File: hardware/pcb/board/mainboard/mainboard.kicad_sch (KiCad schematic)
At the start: 136 parts, among them J1 Conn_Coaxial, J10 USB_C_Receptacle, J11 2908-05WB-MG, J2 USB_C_Receptacle_USB2.0_16P, J3 Conn_02x35_Odd_Even_MountingP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, J4 Conn_02x40_Odd_Even_MountingP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, J5 Conn_02x40_Odd_Even_MountingP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, J7 Conn_01x30, J8 Conn_01x30, J9 Conn_01x30, Q1 BSS138, Q2 DMN3008SFG, Q3 DMN3008SFG, U1 TPS7A20_SOT-23, U11 TPS7A20_SOT-23, U12 AP33771C, U13 TXS0104E, U14 FT234XD-R, U2 LSM6DS3TR, U3 NEO-M8N, U4 BQ25606, U5 BQ27441-G1, U6 SN74LVC1T45DBVR, U7 LIS2MDL, U8 SN74LVC1T45DBVR, U9 TPS61235P

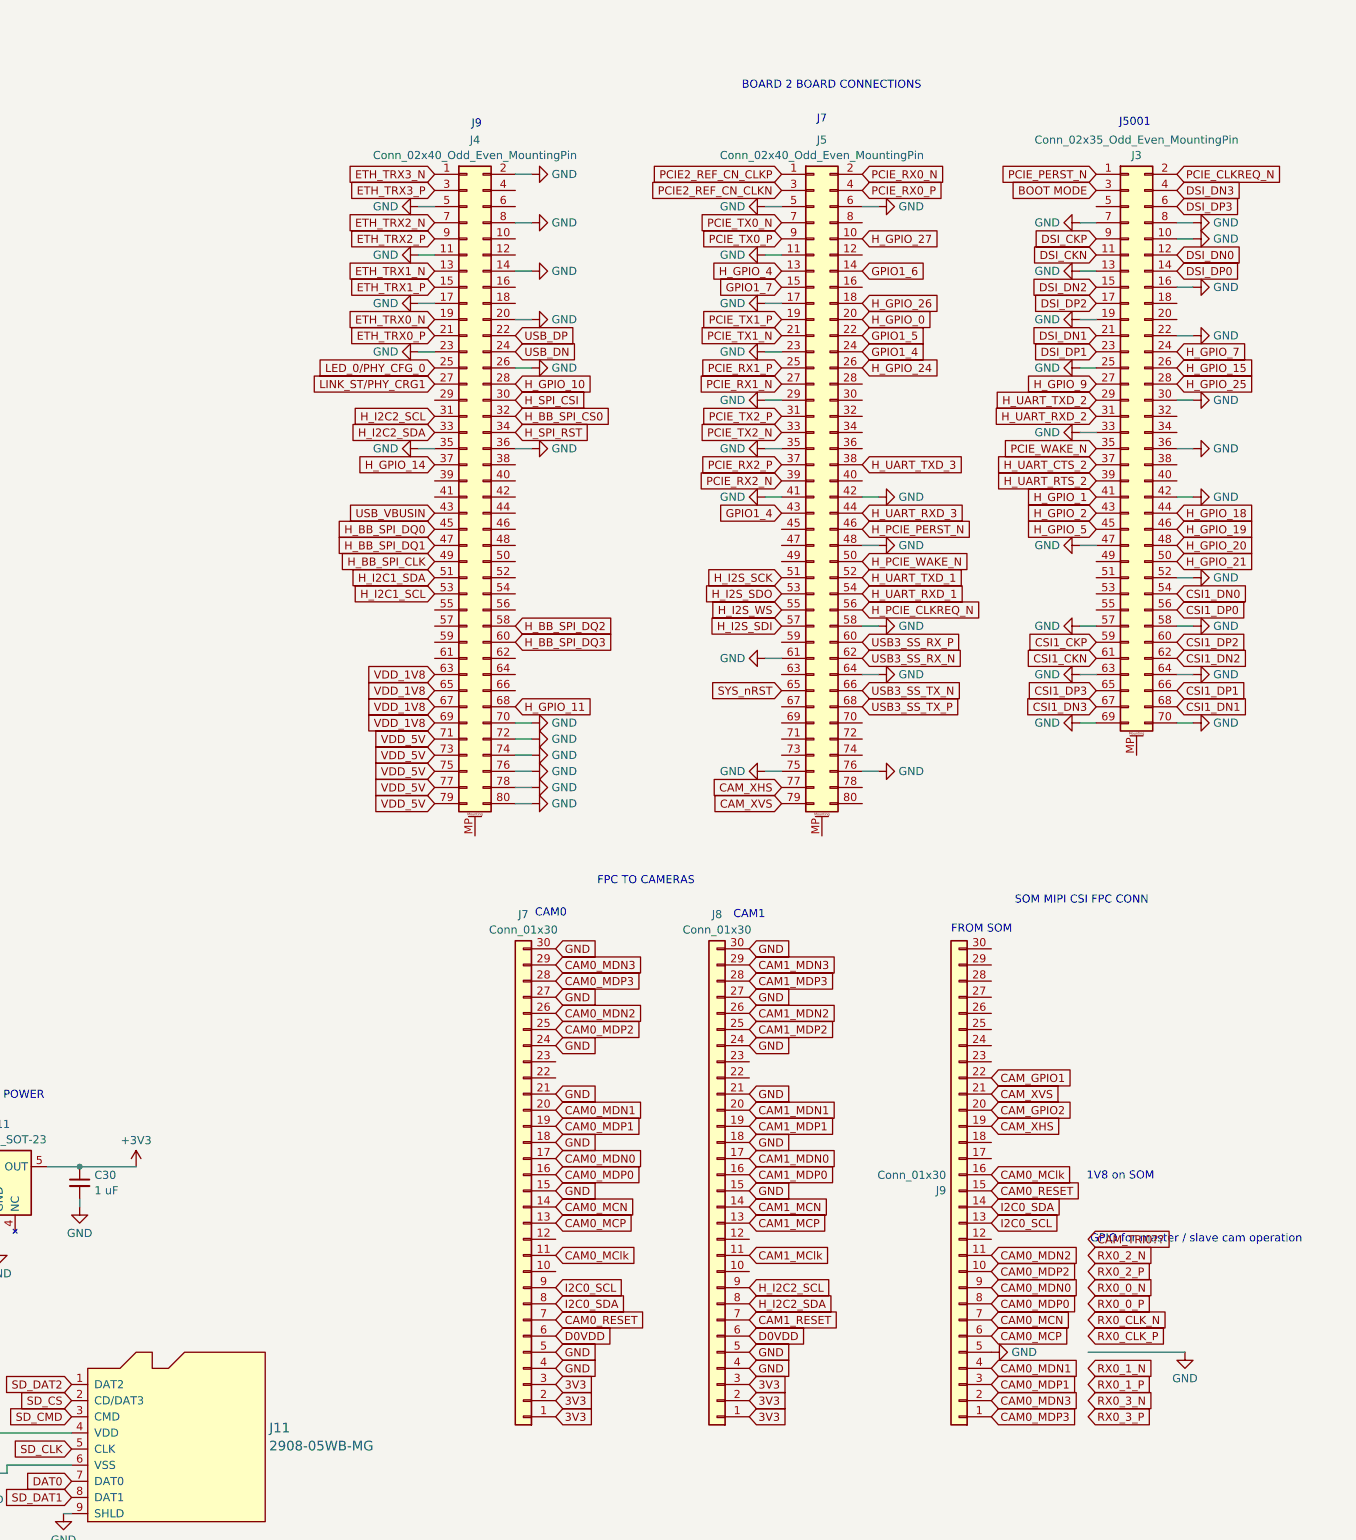
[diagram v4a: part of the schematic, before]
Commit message: change MIPI CSI location according to new schematics
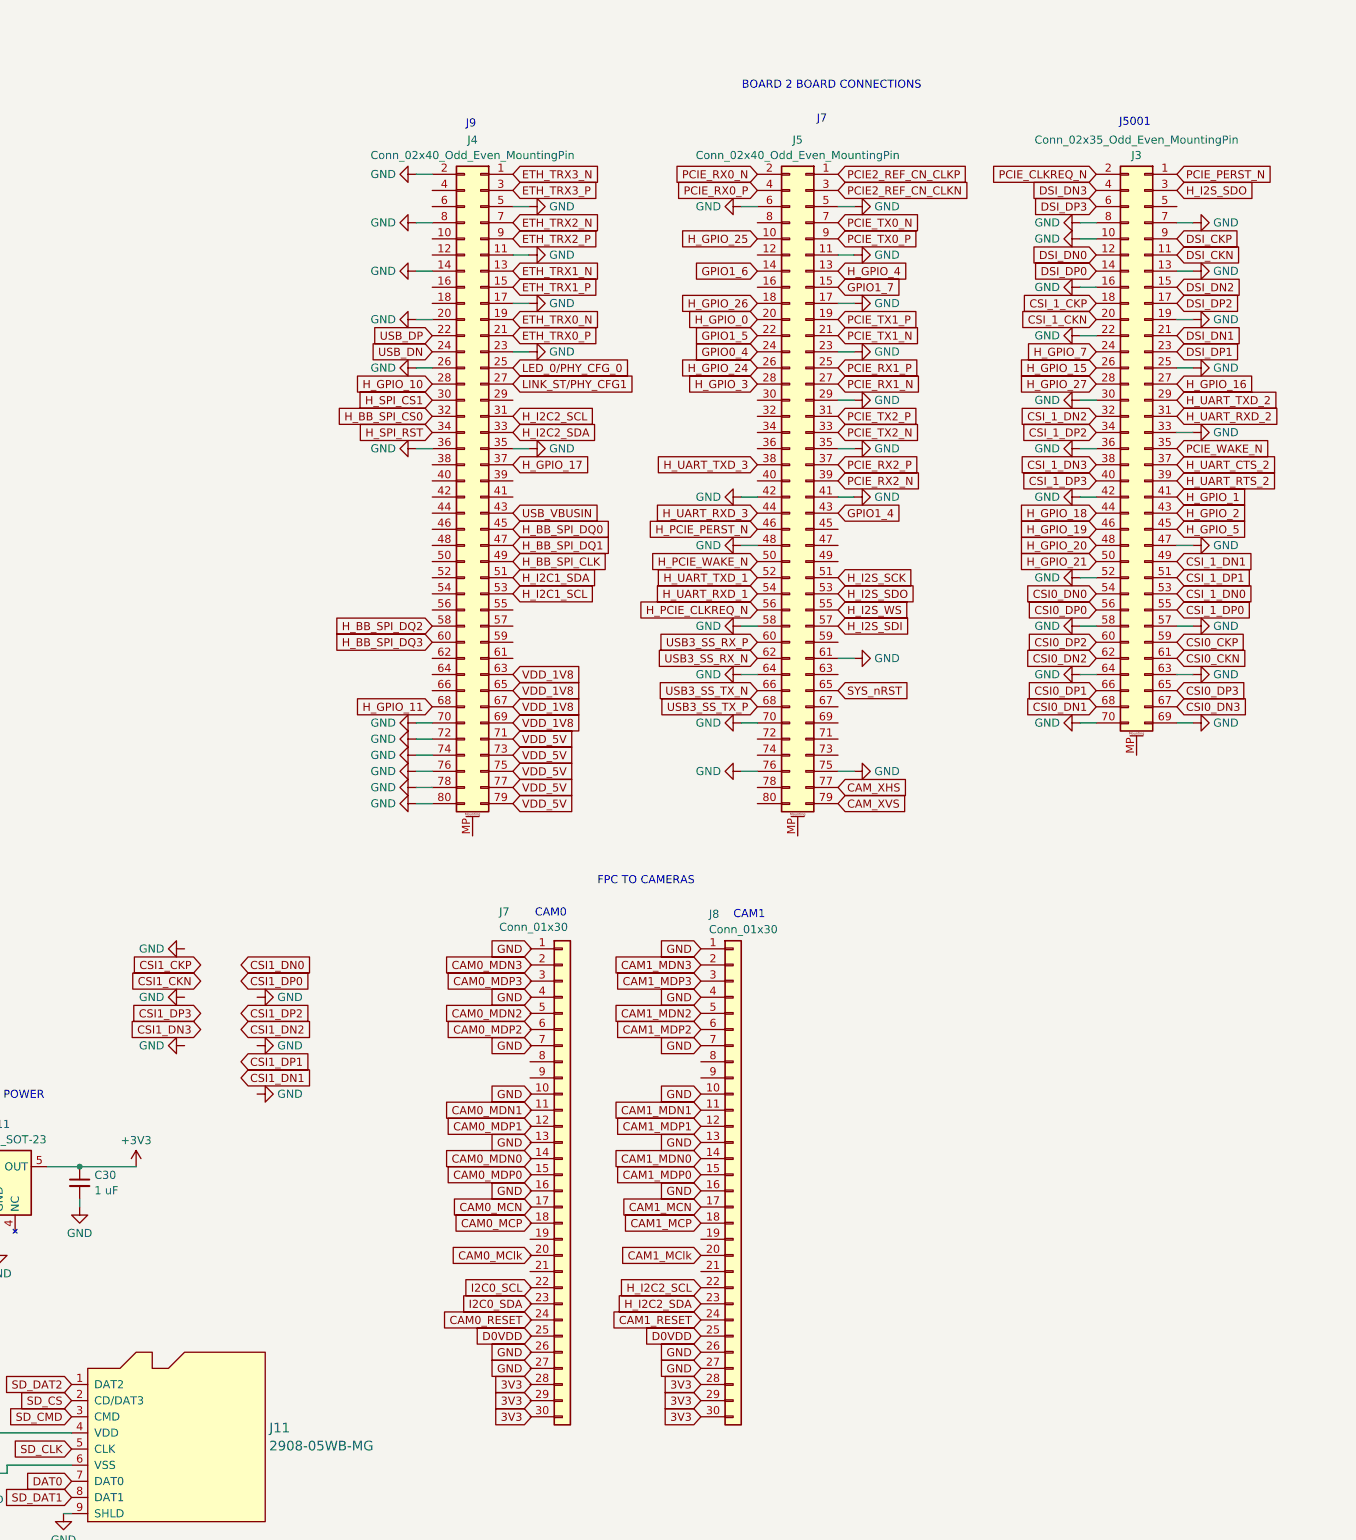
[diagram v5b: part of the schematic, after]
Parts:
- removed J9: Conn_01x30, Connector_FFC-FPC:Hirose_FH12-30S-0.5SH_1x30-1MP_P0.50mm_Horizontal, symbol Connector_Generic:Conn_01x30
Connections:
- net BOOT MODE is gone; now on net H_I2S_SDO: J3.3 (Pin_3)
- net 3V3: now also J8.28 (Pin_28), J8.29 (Pin_29), J8.30 (Pin_30); no longer J7.1 (Pin_1), J7.2 (Pin_2), J7.3 (Pin_3), J8.1 (Pin_1), J8.2 (Pin_2), J8.3 (Pin_3)
- net CAM0_MCN: no longer J7.14 (Pin_14)
- net CAM0_MCP: no longer J7.13 (Pin_13)
- net CAM0_MClk: no longer J7.11 (Pin_11)
- net CAM0_MDN0: no longer J7.17 (Pin_17)
- net CAM0_MDN1: no longer J7.20 (Pin_20)
- net CAM0_MDN2: no longer J7.26 (Pin_26)
- net CAM0_MDN3: no longer J7.29 (Pin_29)
- net CAM0_MDP0: no longer J7.16 (Pin_16)
- net CAM0_MDP1: no longer J7.19 (Pin_19)
- net CAM0_MDP2: no longer J7.25 (Pin_25)
- net CAM0_MDP3: no longer J7.28 (Pin_28)
- net CAM0_RESET: no longer J7.7 (Pin_7)
- net CAM1_MCN: now also J8.17 (Pin_17); no longer J8.14 (Pin_14)
- net CAM1_MCP: now also J8.18 (Pin_18); no longer J8.13 (Pin_13)
- net CAM1_MClk: now also J8.20 (Pin_20); no longer J8.11 (Pin_11)
- net CAM1_MDN0: now also J8.14 (Pin_14); no longer J8.17 (Pin_17)
- net CAM1_MDN1: now also J8.11 (Pin_11); no longer J8.20 (Pin_20)
- net CAM1_MDN2: now also J8.5 (Pin_5); no longer J8.26 (Pin_26)
- net CAM1_MDN3: now also J8.2 (Pin_2); no longer J8.29 (Pin_29)
- net CAM1_MDP0: now also J8.15 (Pin_15); no longer J8.16 (Pin_16)
- net CAM1_MDP1: now also J8.12 (Pin_12); no longer J8.19 (Pin_19)
- net CAM1_MDP2: now also J8.6 (Pin_6); no longer J8.25 (Pin_25)
- net CAM1_MDP3: now also J8.3 (Pin_3); no longer J8.28 (Pin_28)
- net CAM1_RESET: now also J8.24 (Pin_24); no longer J8.7 (Pin_7)
- net CSI1_CKN: no longer J3.61 (Pin_61)
- net CSI1_CKP: no longer J3.59 (Pin_59)
- net CSI1_DN0: no longer J3.54 (Pin_54)
- net CSI1_DN1: no longer J3.68 (Pin_68)
- net CSI1_DN2: no longer J3.62 (Pin_62)
- net CSI1_DN3: no longer J3.67 (Pin_67)
- net CSI1_DP0: no longer J3.56 (Pin_56)
- net CSI1_DP1: no longer J3.66 (Pin_66)
- net CSI1_DP2: no longer J3.60 (Pin_60)
- net CSI1_DP3: no longer J3.65 (Pin_65)
- net D0VDD: now also J8.25 (Pin_25); no longer J7.6 (Pin_6), J8.6 (Pin_6)
- net GND: now also J5.70 (Pin_70), J8.1 (Pin_1), J8.10 (Pin_10), J8.13 (Pin_13), J8.16 (Pin_16), J8.26 (Pin_26), J8.7 (Pin_7); no longer J7.15 (Pin_15), J7.18 (Pin_18), J7.21 (Pin_21), J7.24 (Pin_24), J7.27 (Pin_27), J7.30 (Pin_30), J7.4 (Pin_4), J7.5 (Pin_5), J8.15 (Pin_15), J8.18 (Pin_18), J8.21 (Pin_21), J8.24 (Pin_24), J8.30 (Pin_30), J8.5 (Pin_5)
- net GPIO1_4: no longer J5.24 (Pin_24)
- net H_GPIO_25: now also J5.10 (Pin_10); no longer J3.28 (Pin_28)
- net H_GPIO_27: now also J3.28 (Pin_28); no longer J5.10 (Pin_10)
- net H_I2C2_SCL: now also J8.22 (Pin_22); no longer J8.9 (Pin_9)
- net H_I2C2_SDA: now also J8.23 (Pin_23); no longer J8.8 (Pin_8)
- net I2C0_SCL: no longer J7.9 (Pin_9)
- net I2C0_SDA: no longer J7.8 (Pin_8)
- net CSI_1_CKP: now reaches J3.18 (Pin_18)
- net CSI_1_CKN: now reaches J3.20 (Pin_20)
- net CSI_1_DN2: now reaches J3.32 (Pin_32)
- net CSI_1_DP2: now reaches J3.34 (Pin_34)
- net CSI_1_DN3: now reaches J3.38 (Pin_38)
- net CSI_1_DP3: now reaches J3.40 (Pin_40)
- net CSI_1_DN1: now reaches J3.49 (Pin_49)
- net CSI_1_DP1: now reaches J3.51 (Pin_51)
- net CSI_1_DN0: now reaches J3.53 (Pin_53)
- net CSI_1_DP0: now reaches J3.55 (Pin_55)
- net H_GPIO_3: now reaches J5.28 (Pin_28)
- net H_GPIO_14 renamed H_GPIO_17
- net H_GPIO_9 renamed H_GPIO_16
- net H_SPI_CSI renamed H_SPI_CS1
- net LINK_ST/PHY_CRG1 renamed LINK_ST/PHY_CFG1
- new net CSI0_CKN: J3.61 (Pin_61)
- new net CSI0_CKP: J3.59 (Pin_59)
- new net CSI0_DN0: J3.54 (Pin_54)
- new net CSI0_DN1: J3.68 (Pin_68)
- new net CSI0_DN2: J3.62 (Pin_62)
- new net CSI0_DN3: J3.67 (Pin_67)
- new net CSI0_DP0: J3.56 (Pin_56)
- new net CSI0_DP1: J3.66 (Pin_66)
- new net CSI0_DP2: J3.60 (Pin_60)
- new net CSI0_DP3: J3.65 (Pin_65)
- new net GPIO0_4: J5.24 (Pin_24)
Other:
- note removed: "1V8 on SOM"
- note removed: "FROM SOM"
- note removed: "GPIO for master / slave cam operation"
- note removed: "SOM MIPI CSI FPC CONN"
- moved on the sheet: J5, J7, J8

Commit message: new 3V3 setup for cameras, 30 pin mipi connections
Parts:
- removed C29, C30: 1 uF, Capacitor_SMD:C_0603_1608Metric, symbol Device:C_Small
- removed U11: TPS7A20_SOT-23, Package_SON:Texas_X2SON-4_1x1mm_P0.65mm, symbol unsurv_offline_pcb_symbols:TPS7A20_SOT-23
- added C43, C44, C45, C46: 4.7 uF, Capacitor_SMD:C_0603_1608Metric, symbol Device:C_Small
- added R21, R33, R36: 0, Resistor_SMD:R_0603_1608Metric, symbol Device:R_Small
- added R34, R35: 10k, Resistor_SMD:R_0603_1608Metric, symbol Device:R_Small
- added U10, U11: AP2114H-3_3TRG1, digikey-footprints:SOT-223, symbol dk_PMIC-Voltage-Regulators-Linear:AP2114H-3_3TRG1
- added Y1, Y2: SiT8008xx-1x-xxE, Oscillator:Oscillator_SMD_SiT_PQFN-4Pin_2.5x2.0mm, symbol Oscillator:SiT8008xx-1x-xxE
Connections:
- net CAM1_RESET is gone; now on net CAM0_RESET: J8.24 (Pin_24)
- net H_GPIO_19 is gone; now on net CAM0_RESET: J3.46 (Pin_46)
- net VDD_5V is gone; now on net +5V: J4.71 (Pin_71), J4.73 (Pin_73), J4.75 (Pin_75), J4.77 (Pin_77), J4.79 (Pin_79)
- net +5V: now also C43.1, C45.1, U10.3 (IN), U11.3 (IN)
- net CAM0_MClk: now also J7.20 (Pin_20), R21.2
- net CAM0_RESET: now also R34.1, R35.2, R36.1
- net CAM1_MCN: no longer J8.17 (Pin_17)
- net CAM1_MCP: no longer J8.18 (Pin_18)
- net CAM1_MClk: now also R33.2
- net CAM1_MDN0: no longer J8.14 (Pin_14)
- net CAM1_MDN1: no longer J8.11 (Pin_11)
- net CAM1_MDN2: no longer J8.5 (Pin_5)
- net CAM1_MDN3: no longer J8.2 (Pin_2)
- net CAM1_MDP0: no longer J8.15 (Pin_15)
- net CAM1_MDP1: no longer J8.12 (Pin_12)
- net CAM1_MDP2: no longer J8.6 (Pin_6)
- net CAM1_MDP3: no longer J8.3 (Pin_3)
- net CSI0_CKN: now also J7.17 (Pin_17)
- net CSI0_CKP: now also J7.18 (Pin_18)
- net CSI0_DN0: now also J7.14 (Pin_14)
- net CSI0_DN1: now also J7.11 (Pin_11)
- net CSI0_DN2: now also J7.5 (Pin_5)
- net CSI0_DN3: now also J7.2 (Pin_2)
- net CSI0_DP0: now also J7.15 (Pin_15)
- net CSI0_DP1: now also J7.12 (Pin_12)
- net CSI0_DP2: now also J7.6 (Pin_6)
- net CSI0_DP3: now also J7.3 (Pin_3)
- net CSI_1_CKN: now also J8.17 (Pin_17)
- net CSI_1_CKP: now also J8.18 (Pin_18)
- net CSI_1_DN0: now also J8.14 (Pin_14)
- net CSI_1_DN1: now also J8.11 (Pin_11)
- net CSI_1_DN2: now also J8.5 (Pin_5)
- net CSI_1_DN3: now also J8.2 (Pin_2)
- net CSI_1_DP0: now also J8.15 (Pin_15)
- net CSI_1_DP1: now also J8.12 (Pin_12)
- net CSI_1_DP2: now also J8.6 (Pin_6)
- net CSI_1_DP3: now also J8.3 (Pin_3)
- net D0VDD: no longer J8.25 (Pin_25)
- net GND: now also J7.1 (Pin_1), J7.10 (Pin_10), J7.13 (Pin_13), J7.16 (Pin_16), J7.26 (Pin_26), J7.27 (Pin_27), J7.4 (Pin_4), J7.7 (Pin_7), C43.2, C44.2, C45.2, C46.2, R35.1, U10.1 (GND), U11.1 (GND), Y1.2 (GND), Y2.2 (GND)
- net I2C0_SCL: now also J7.22 (Pin_22)
- net I2C0_SDA: now also J7.23 (Pin_23)
- net VDD_1V8: now also J7.25 (Pin_25), J8.25 (Pin_25), R34.2, Y1.1 (OE), Y1.4 (Vdd), Y2.1 (OE), Y2.4 (Vdd)
- net at J7.24 (Pin_24): now also R36.2
- net CAM0_3V3: now reaches J7.28 (Pin_28)
- net CAM0_3V3: now also J7.29 (Pin_29), J7.30 (Pin_30), C44.1, U10.2 (VOUT), U10.4 (VOUT)
- net 3V3 renamed CAM1_3V3
- net CAM1_3V3: now also C46.1, U11.2 (VOUT), U11.4 (VOUT)
- new net: R33.1, Y2.3 (OUT)
- new net: R21.1, Y1.3 (OUT)
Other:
- note added: "# TODO - check coax conn type for antennas - TP everything! - 0 ohm connections - add way for cam0 cam1 slave master operation? - TXS0102 logic lvl shifter - WATCH FOR INVERSE PINS WHEN SWITCHING SIDE FOR CAM 0 / 1 - transfer SOM based MIPI to CAM connection via FPC - CAM CLK crystal , 0 Ohm, 25 MHz, 25 ppm, 1.8V"
- note added: "CAM 3V3 POWER"
- note removed: "# TODO - check coax conn type for antennas - TP everything! - 0 ohm connections - add way for cam0 cam1 slave master operation? - TXS0102 logic lvl shifter - WATCH FOR INVERSE PINS WHEN SWITCHING SIDE FOR CAM 0 / 1 - transfer SOM based MIPI to CAM connection via FPC"
- note removed: "2nd 3V3 POWER"
- moved on the sheet: C37, J11, J8, R30, R31

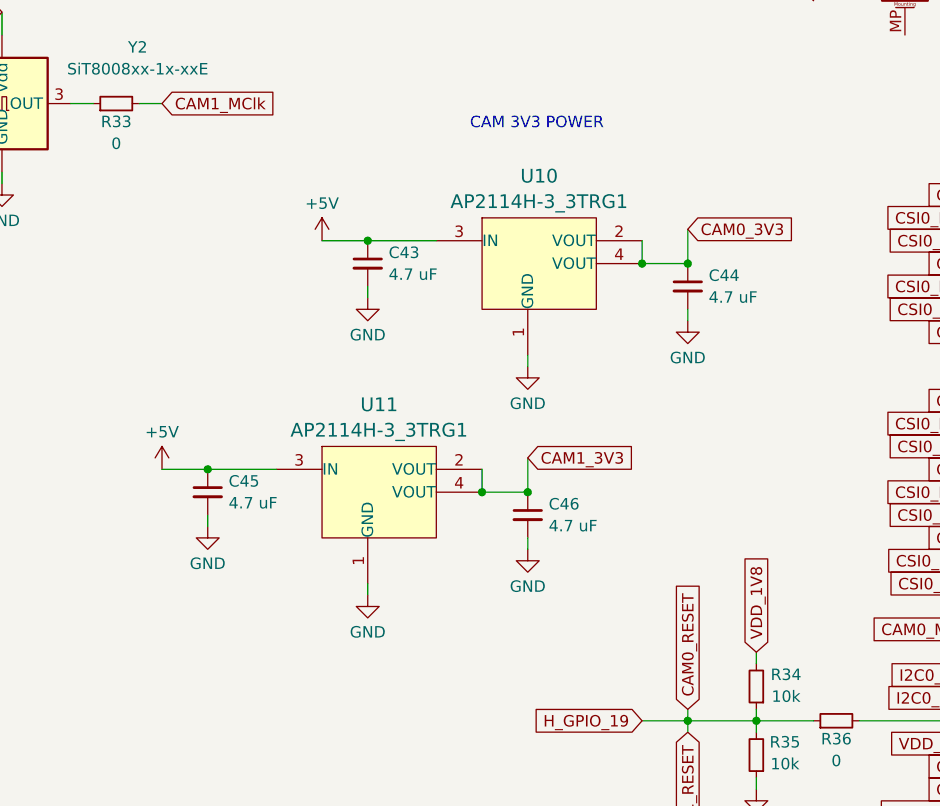
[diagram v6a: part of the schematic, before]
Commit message: place ment of new 3V3 + oscillators + reset mechanic
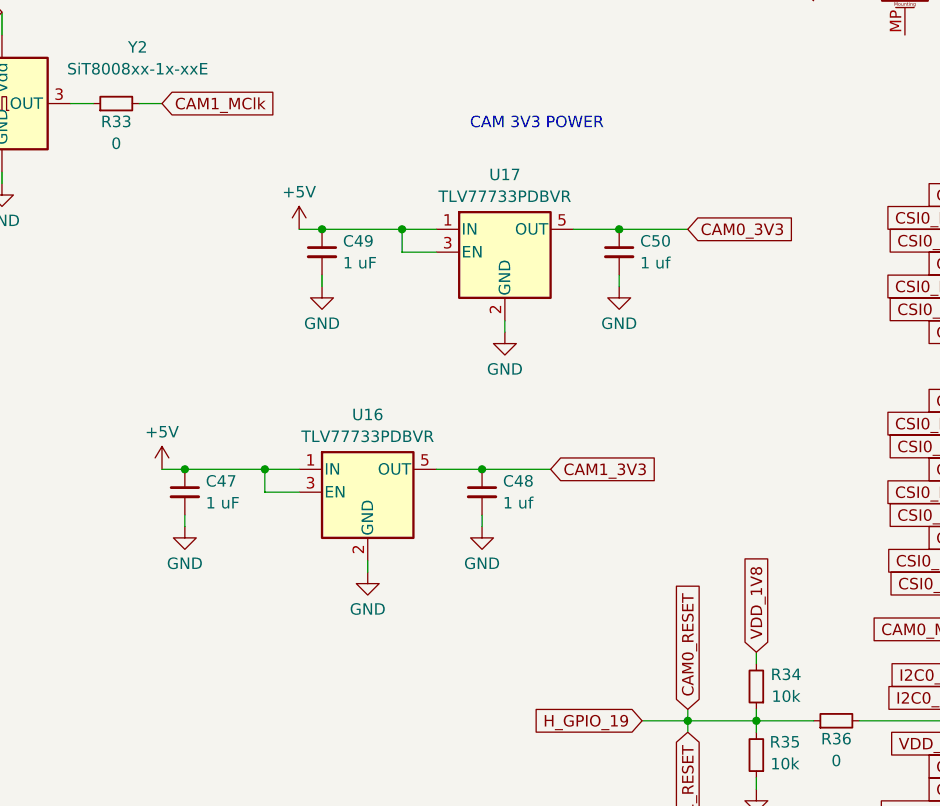
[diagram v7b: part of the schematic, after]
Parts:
- removed C43, C44, C45, C46: 4.7 uF, Capacitor_SMD:C_0603_1608Metric, symbol Device:C_Small
- removed U10, U11: AP2114H-3_3TRG1, digikey-footprints:SOT-223, symbol dk_PMIC-Voltage-Regulators-Linear:AP2114H-3_3TRG1
- added C47, C49: 1 uF, Capacitor_SMD:C_0603_1608Metric, symbol Device:C_Small
- added C48, C50: 1 uf, Capacitor_SMD:C_0603_1608Metric, symbol Device:C_Small
- added U16, U17: TLV77733PDBVR, Package_TO_SOT_SMD:SOT-23-5, symbol Regulator_Linear:TLV70032_SOT23-5
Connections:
- net +5V: now also C47.1, C49.1, U16.1 (IN), U16.3 (EN), U17.1 (IN), U17.3 (EN)
- net CAM0_3V3: now also C50.1, U17.5 (OUT)
- net CAM1_3V3: now also C48.1, U16.5 (OUT)
- net GND: now also C47.2, C48.2, C49.2, C50.2, U16.2 (GND), U17.2 (GND)

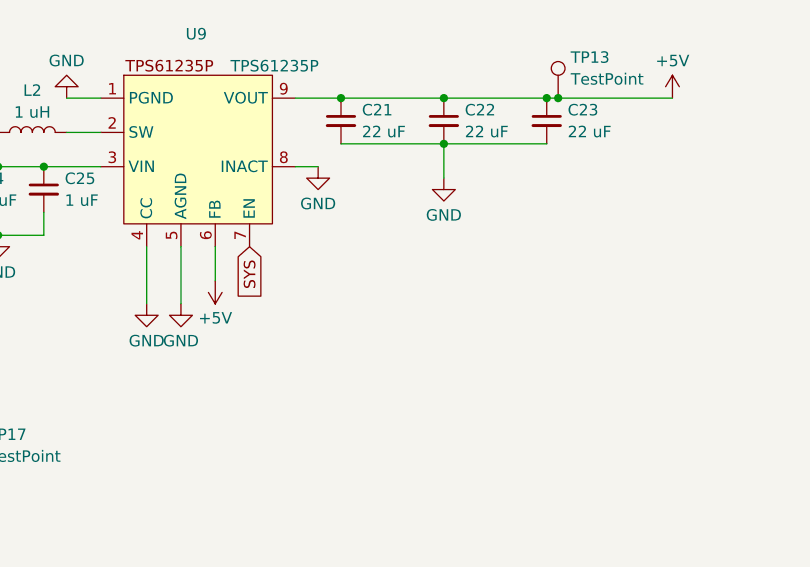
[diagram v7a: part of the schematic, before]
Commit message: cam1 MIPI pairs
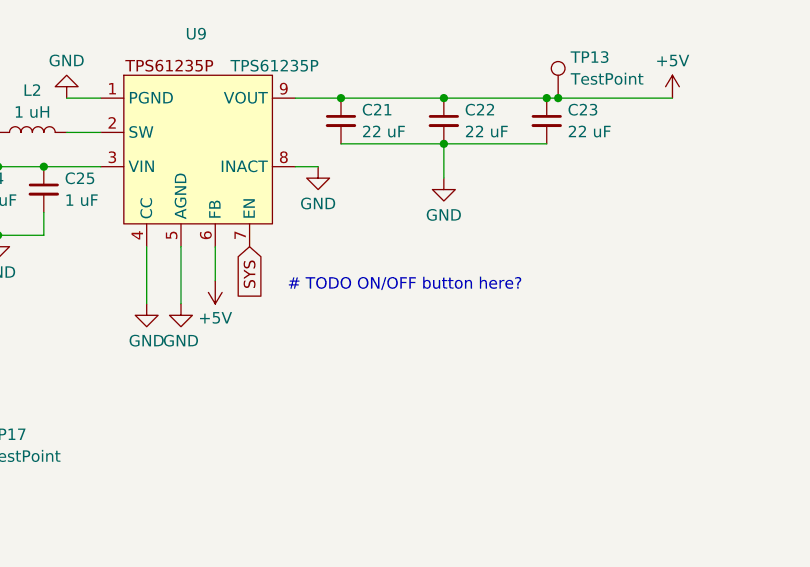
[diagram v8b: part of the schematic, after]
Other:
- note added: "# TODO ON/OFF button here?"
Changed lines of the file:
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@@
+		)
+	)
+	(text "# TODO ON/OFF button here?"
+		(exclude_from_sim no)
+		(at 90.932 163.068 0)
+		(effects
+			(font
+				(size 1.27 1.27)
+			)
 		)
 	)
